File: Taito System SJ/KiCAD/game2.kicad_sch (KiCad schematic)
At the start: 5 parts, among them U47 74LS153, U58 74LS04

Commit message: Added first 3 sound chips
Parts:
- added C?: 10uF, symbol Device:C_Polarized_Small
- added C? (x2): 47pF, symbol Device:C_Small
- added C? (x3): 1uF, symbol Device:C_Small
- added C?: 0.022uF, symbol Device:C_Small
- added C? (x3): 0.1uF, symbol Device:C_Polarized_Small
- added C? (x2): 1uF, symbol Device:C_Polarized_Small
- added R? (x3): 1K, symbol Device:R_US
- added R? (x8): 30K, symbol Device:R_US
- added R? (x9): 1M, symbol Device:R_US
- added R? (x5): 10K, symbol Device:R_US
- added R? (x8): 15K, symbol Device:R_US
- added R?: 39K, symbol Device:R_US
- added R?: 150K, symbol Device:R_US
- added R?: 330K, symbol Device:R_US
- added R?: 2.2M, symbol Device:R_US
- added R?: 82K, symbol Device:R_US
- added R?: 270, symbol Device:R_US
- added R?: 4.7K, symbol Device:R_US
- added R?: 270K, symbol Device:R_US
- added R?: 20K, symbol Device:R_US
- added R?: 3.9K, symbol Device:R_US
- added R?: 680K, symbol Device:R_US
- added TP?: PSG2, symbol Connector:TestPoint
- added TP?: PSG4, symbol Connector:TestPoint
- added TP?: PSG3, symbol Connector:TestPoint
- added TP?: DAOUT, symbol Connector:TestPoint
- added TP?: PSG1, symbol Connector:TestPoint
- added U17, U8: HA17301, symbol arcade:HA17301
- added unit 3 of U58
- gave numbers to parts that had none: 3
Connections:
- net GNDPWR: now also C?.2, C?.2, R?.1, R?.1, R?.1, R?.2, R?.2
- net VCC: now also U50.25 (A8), R?.1
- net at U51.10 (IOB3): now also R?.2
- net at U51.11 (IOB2): now also R?.2
- net at U51.12 (IOB1): now also R?.2
- net at U51.13 (IOB0): now also R?.2
- net at U51.14 (IOA7): now also R?.2
- net at U51.15 (IOA6): now also R?.2
- net at U51.16 (IOA5): now also R?.2
- net at U51.17 (IOA4): now also R?.2
- net at U51.18 (IOA3): now also R?.2
- net at U51.19 (IOA2): now also R?.2
- net at U51.20 (IOA1): now also R?.2
- net at U51.21 (IOA0): now also R?.2
- net AB1: now reaches U51.24 (~{A9})
- net AB1: now also U49.24 (~{A9}), U49.25 (A8)
- net at U51.25 (A8): now also U50.24 (~{A9}), U58.6
- net at U51.3 (CHB): now also U51.38 (CHC), U51.4 (CHA), R?.2, R?.2
- net at U51.6 (IOB7): now also R?.2
- net at U51.7 (IOB6): now also R?.2
- net at U51.8 (IOB5): now also R?.2
- net at U51.9 (IOB4): now also R?.2
- net IN57: now reaches U49.14 (IOA7)
- net IN56: now reaches U49.15 (IOA6)
- net IN55: now reaches U49.16 (IOA5)
- net IN54: now reaches U49.17 (IOA4)
- net at U49.3 (CHB): now also U49.38 (CHC), U49.4 (CHA), R?.2, R?.2
- net CIOB0: now reaches U50.13 (IOB0)
- net at U50.20 (IOA1): now also C?.1
- net at U50.21 (IOA0): now also C?.1
- net at U50.3 (CHB): now also U50.38 (CHC), U50.4 (CHA), C?.1, R?.2
- net ~{RESET} renamed ~{RESET1}
- new net: R?.1, R?.1, R?.2 (x7)
- new net: C?.1, C?.2, R?.1, U8.4
- new net: R?.1, R?.2, R?.2
- new net: C?.1, C?.2, R?.1, TP?.1, U17.4
- new net: C?.2, C?.2, R?.1, R?.2, R?.2
- new net: C?.1, R?.1 (x2)
- new net: C?.2, R?.2 (x2)
- new net: R?.1, U17.2 (+)
- new net: C?.1, R?.1, U17.3 (-)
- new net: R?.1, U8.2 (+)
- new net: C?.1, R?.1, U8.3 (-)
- new net: C?.1, R?.1, TP?.1, U8.9
- new net: C?.1, R?.1, R?.1, R?.1, R?.1, R?.1, R?.1, R?.1, R?.1, R?.1, R?.2, TP?.1
- new net: R?.2, U8.8 (-)
- new net: R?.2, U8.1 (+)
- new net: R?.1, R?.2, U8.5
- new net: R?.2, U8.6 (-)
- new net: R?.1, R?.1, R?.1
- new net 2.5V1: C?.1, R?.1, R?.1, R?.2, R?.2, R?.2, U8.13 (+)
- new net AB2: U58.5
- new net OUT1: C?.2, TP?.1
- new net OUT2: C?.2
- new net OUT3: C?.2, TP?.1
- new net OUT4: C?.2
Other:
- moved on the sheet: U47, U49, U50, U51, U58D, U58E

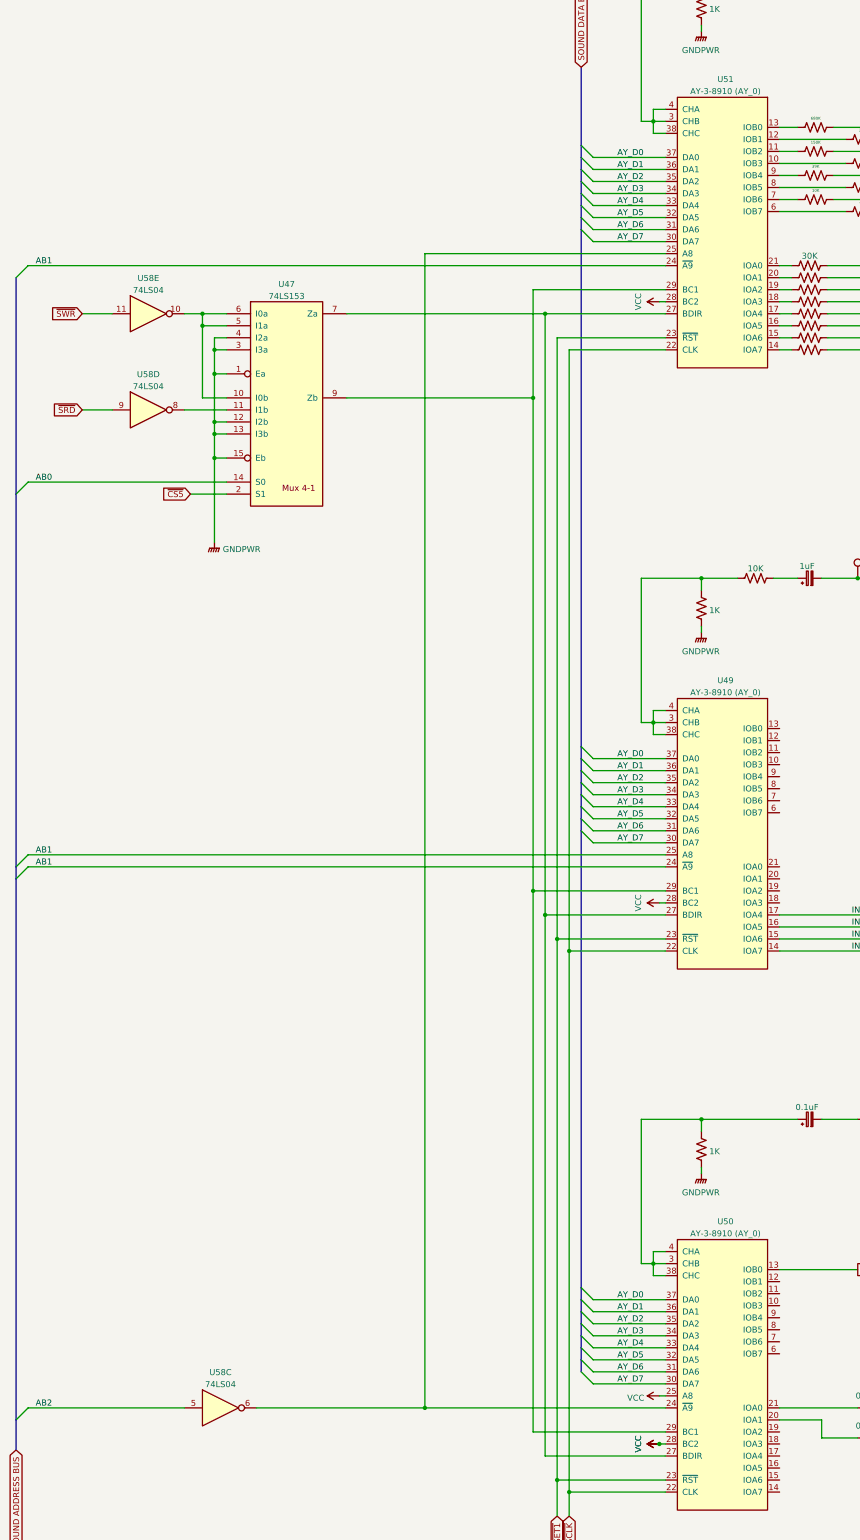
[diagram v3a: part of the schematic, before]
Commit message: Component naming updates
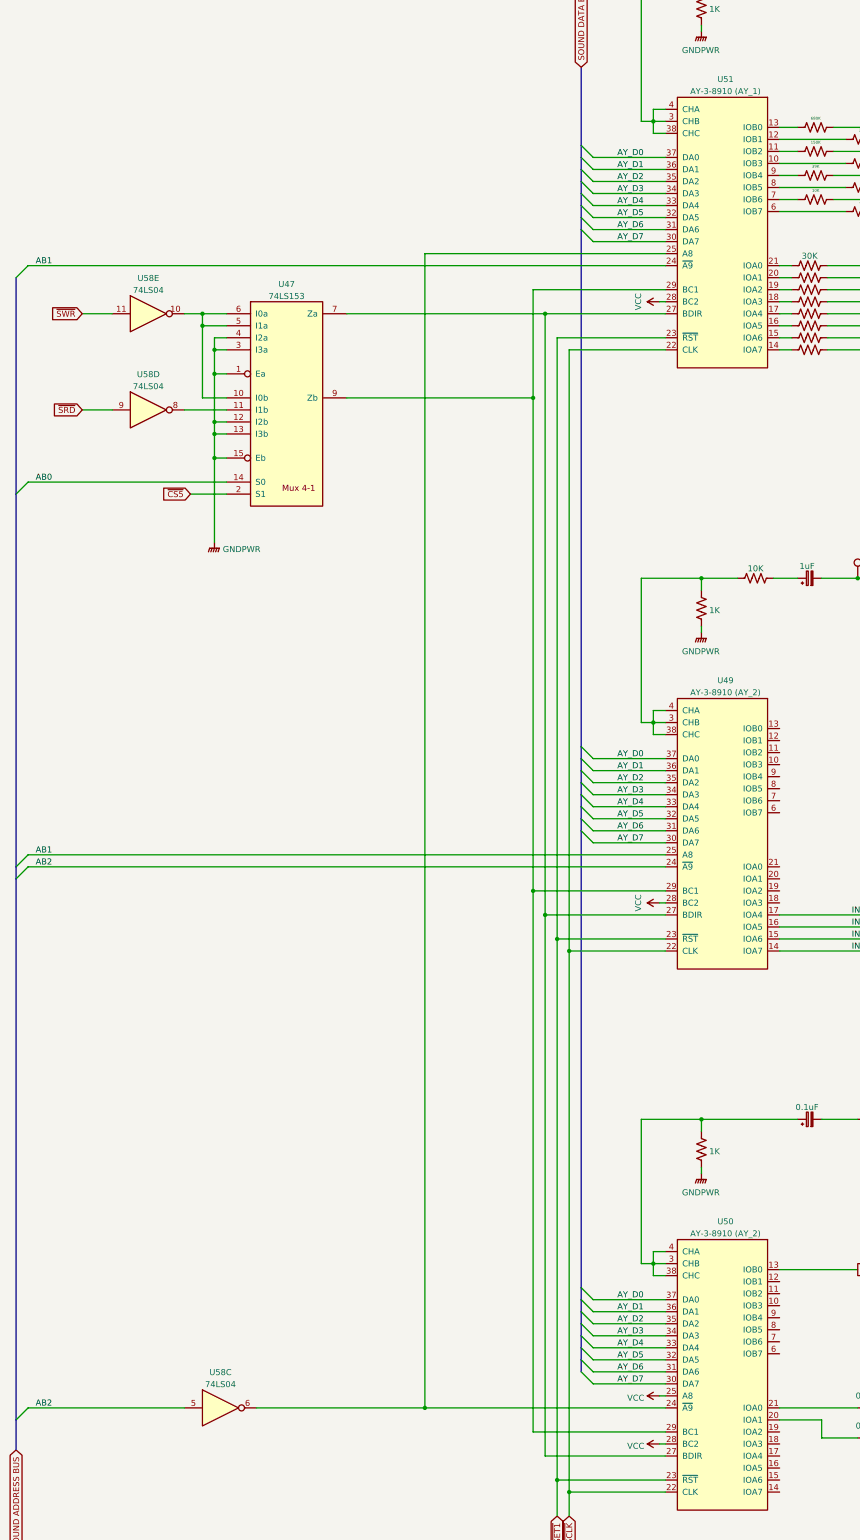
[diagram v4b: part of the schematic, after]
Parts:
- U49, U50: value AY-3-8910 (AY_0) -> AY-3-8910 (AY_2)
- U51: value AY-3-8910 (AY_0) -> AY-3-8910 (AY_1)
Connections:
- net AB1: no longer U49.24 (~{A9})
- net AB2: now also U49.24 (~{A9})
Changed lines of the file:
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@@
   (junction (at 299.72 99.06) (diameter 0) (color 0 0 0 0)
   )
-  (junction (at 207.01 347.98) (diameter 0) (color 0 0 0 0)
-  )
   (junction (at 157.48 340.36) (diameter 0) (color 0 0 0 0)
   )
@@
     (stroke (width 0) (type default))
   )
-  (wire (pts (xy 208.28 347.98) (xy 207.01 347.98))
-    (stroke (width 0) (type default))
-  )
   (wire (pts (xy 208.28 322.58) (xy 193.04 322.58))
     (stroke (width 0) (type default))
@@
     (stroke (width 0) (type default))
   )
+  (wire (pts (xy 207.01 347.98) (xy 208.28 347.98))
+    (stroke (width 0) (type default))
+  )
   (wire (pts (xy 208.28 205.74) (xy 193.04 205.74))
     (stroke (width 0) (type default))
@@
     (effects (font (size 1.27 1.27)) (justify left bottom))
   )
-  (label "AB1" (at 78.74 226.06 180) (fields_autoplaced)
+  (label "AB2" (at 78.74 226.06 180) (fields_autoplaced)
     (effects (font (size 1.27 1.27)) (justify right bottom))
   )
@@
       (effects (font (size 1.2446 1.2446)))
     )
-    (property "Value" "AY-3-8910 (AY_0)" (at 220.98 62.23 0)
+    (property "Value" "AY-3-8910 (AY_1)" (at 220.98 62.23 0)
       (effects (font (size 1.2446 1.2446)))
     )
@@
     )
   )
-  (symbol (lib_id "power:VCC") (at 207.01 347.98 90) (unit 1)
-    (in_bom yes) (on_board yes) (dnp no) (fields_autoplaced)
-    (property "Reference" "#PWR?" (at 210.82 347.98 0)
-      (effects (font (size 1.27 1.27)) hide)
-    )
-    (property "Value" "VCC" (at 202.5666 347.98 0)
-      (effects (font (size 1.27 1.27)))
-    )
-    (property "Footprint" "" (at 207.01 347.98 0)
-      (effects (font (size 1.27 1.27)) hide)
-    )
-    (property "Datasheet" "" (at 207.01 347.98 0)
-      (effects (font (size 1.27 1.27)) hide)
-    )
-    (pin "1")
-    (instances
-      (project "TAITOSJ"
-        (path "/c9398d89-67dd-4ff5-9367-82e2b6879830/a0846401-3d48-4731-bb40-bafe49b0341f"
-          (reference "#PWR?") (unit 1)
-        )
-      )
-    )
-  )
   (symbol (lib_id "arcade:HA17301") (at 386.08 97.79 0) (mirror x) (unit 2)
     (in_bom yes) (on_board yes) (dnp no) (fields_autoplaced)
@@
     )
   )
-  (symbol (lib_id "power:VCC") (at 207.01 347.98 90) (unit 1)
-    (in_bom yes) (on_board yes) (dnp no) (fields_autoplaced)
-    (property "Reference" "#PWR?" (at 210.82 347.98 0)
-      (effects (font (size 1.27 1.27)) hide)
-    )
-    (property "Value" "VCC" (at 202.5666 347.98 0)
-      (effects (font (size 1.27 1.27)))
-    )
-    (property "Footprint" "" (at 207.01 347.98 0)
-      (effects (font (size 1.27 1.27)) hide)
-    )
-    (property "Datasheet" "" (at 207.01 347.98 0)
-      (effects (font (size 1.27 1.27)) hide)
-    )
-    (pin "1")
-    (instances
-      (project "TAITOSJ"
-        (path "/c9398d89-67dd-4ff5-9367-82e2b6879830/a0846401-3d48-4731-bb40-bafe49b0341f"
-          (reference "#PWR?") (unit 1)
-        )
-      )
-    )
-  )
   (symbol (lib_id "Device:R_US") (at 227.33 38.1 270) (unit 1)
     (in_bom yes) (on_board yes) (dnp no) (fields_autoplaced)
@@
       (effects (font (size 1.2446 1.2446)))
     )
-    (property "Value" "AY-3-8910 (AY_0)" (at 220.98 189.23 0)
+    (property "Value" "AY-3-8910 (AY_2)" (at 220.98 189.23 0)
       (effects (font (size 1.2446 1.2446)))
     )
@@
     )
   )
+  (symbol (lib_id "power:VCC") (at 207.01 347.98 90) (unit 1)
+    (in_bom yes) (on_board yes) (dnp no) (fields_autoplaced)
+    (property "Reference" "#PWR09" (at 210.82 347.98 0)
+      (effects (font (size 1.27 1.27)) hide)
+    )
+    (property "Value" "VCC" (at 203.835 348.4138 90)
+      (effects (font (size 1.27 1.27)) (justify left))
+    )
+    (property "Footprint" "" (at 207.01 347.98 0)
+      (effects (font (size 1.27 1.27)) hide)
+    )
+    (property "Datasheet" "" (at 207.01 347.98 0)
+      (effects (font (size 1.27 1.27)) hide)
+    )
+    (pin "1")
+    (instances
+      (project "TAITOSJ"
+        (path "/c9398d89-67dd-4ff5-9367-82e2b6879830/a0846401-3d48-4731-bb40-bafe49b0341f"
+          (reference "#PWR09") (unit 1)
+        )
+      )
+    )
+  )
   (symbol (lib_name "AY-3-8910_1") (lib_id "arcade:AY-3-8910") (at 219.71 330.2 0) (mirror y) (unit 1)
     (in_bom yes) (on_board yes) (dnp no)
@@
       (effects (font (size 1.2446 1.2446)))
     )
-    (property "Value" "AY-3-8910 (AY_0)" (at 220.98 303.53 0)
+    (property "Value" "AY-3-8910 (AY_2)" (at 220.98 303.53 0)
       (effects (font (size 1.2446 1.2446)))
     )

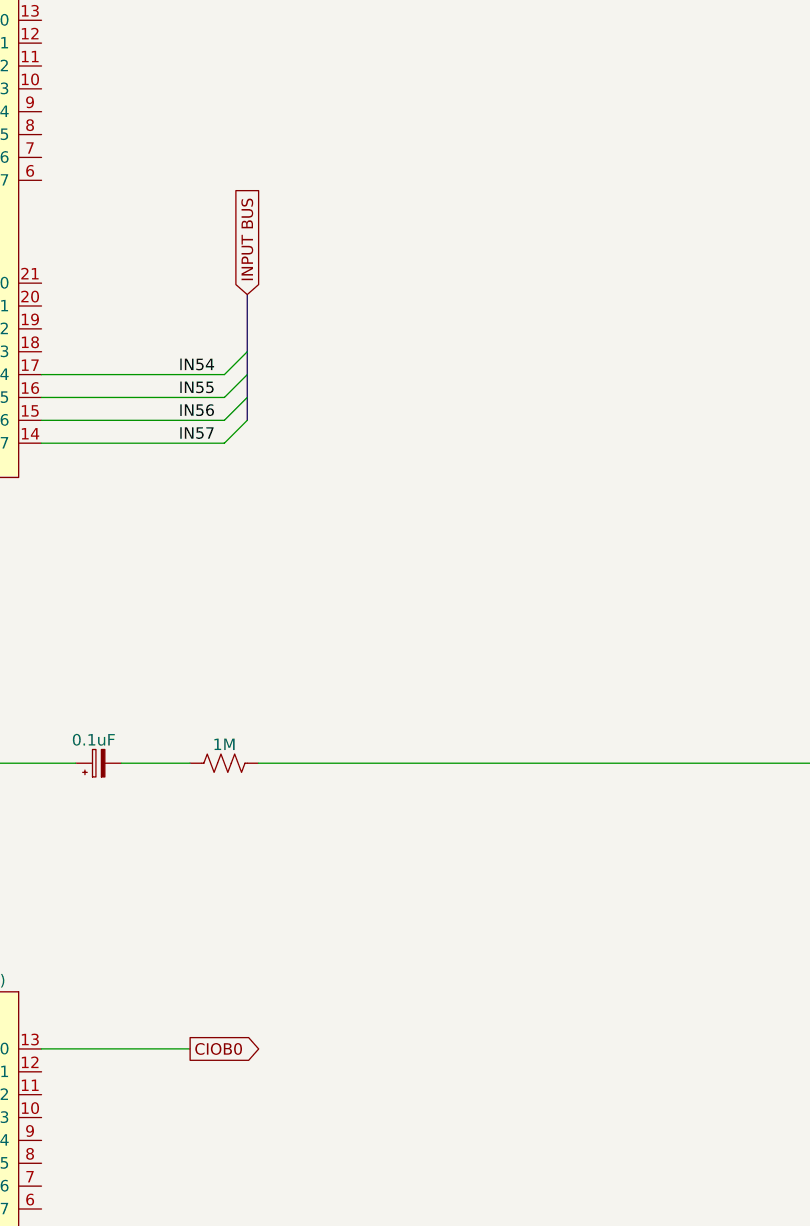
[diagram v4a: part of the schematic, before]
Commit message: Added MCU to Taito SJ Schematics
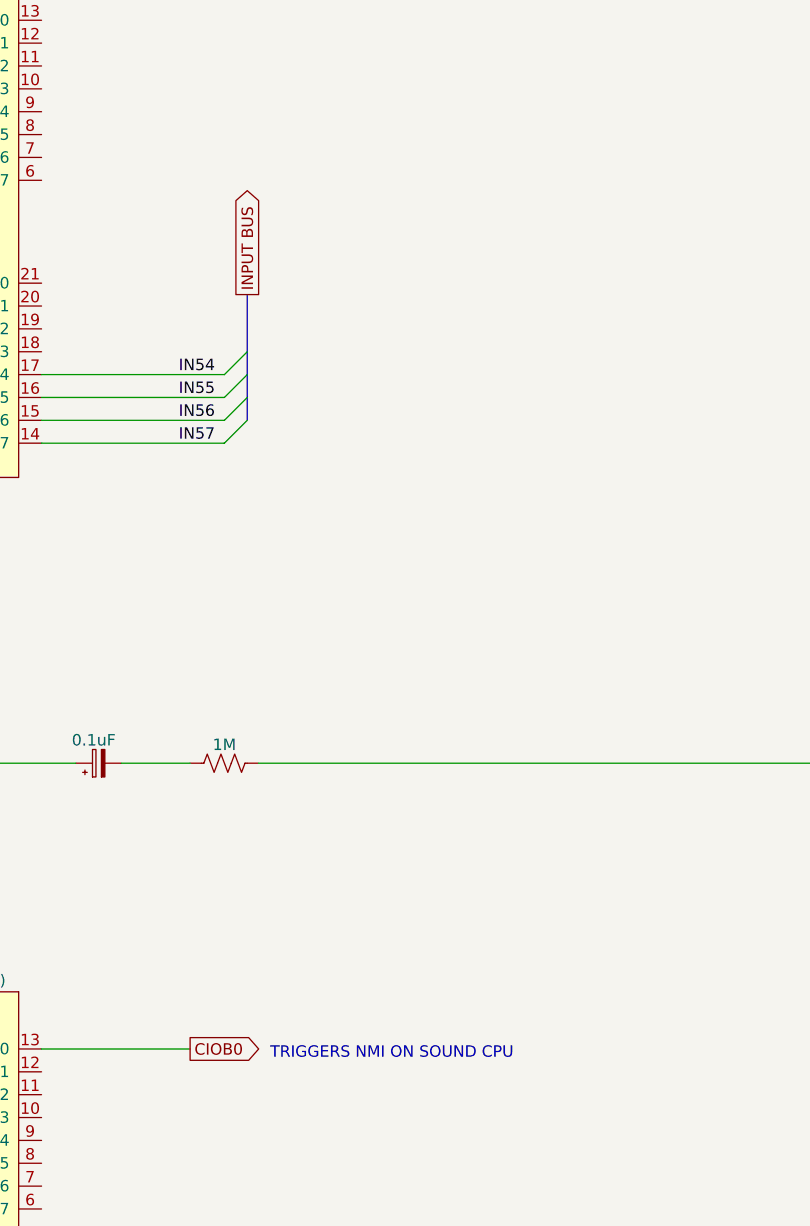
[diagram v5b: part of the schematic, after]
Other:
- note added: "TRIGGERS NMI ON SOUND CPU"
